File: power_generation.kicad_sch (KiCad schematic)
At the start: 36 parts, among them J301 61300211121, J302 61300211121, J303 36103505, J304 36103505, U301 AP64500SP-13, U302 AP64500SP-13

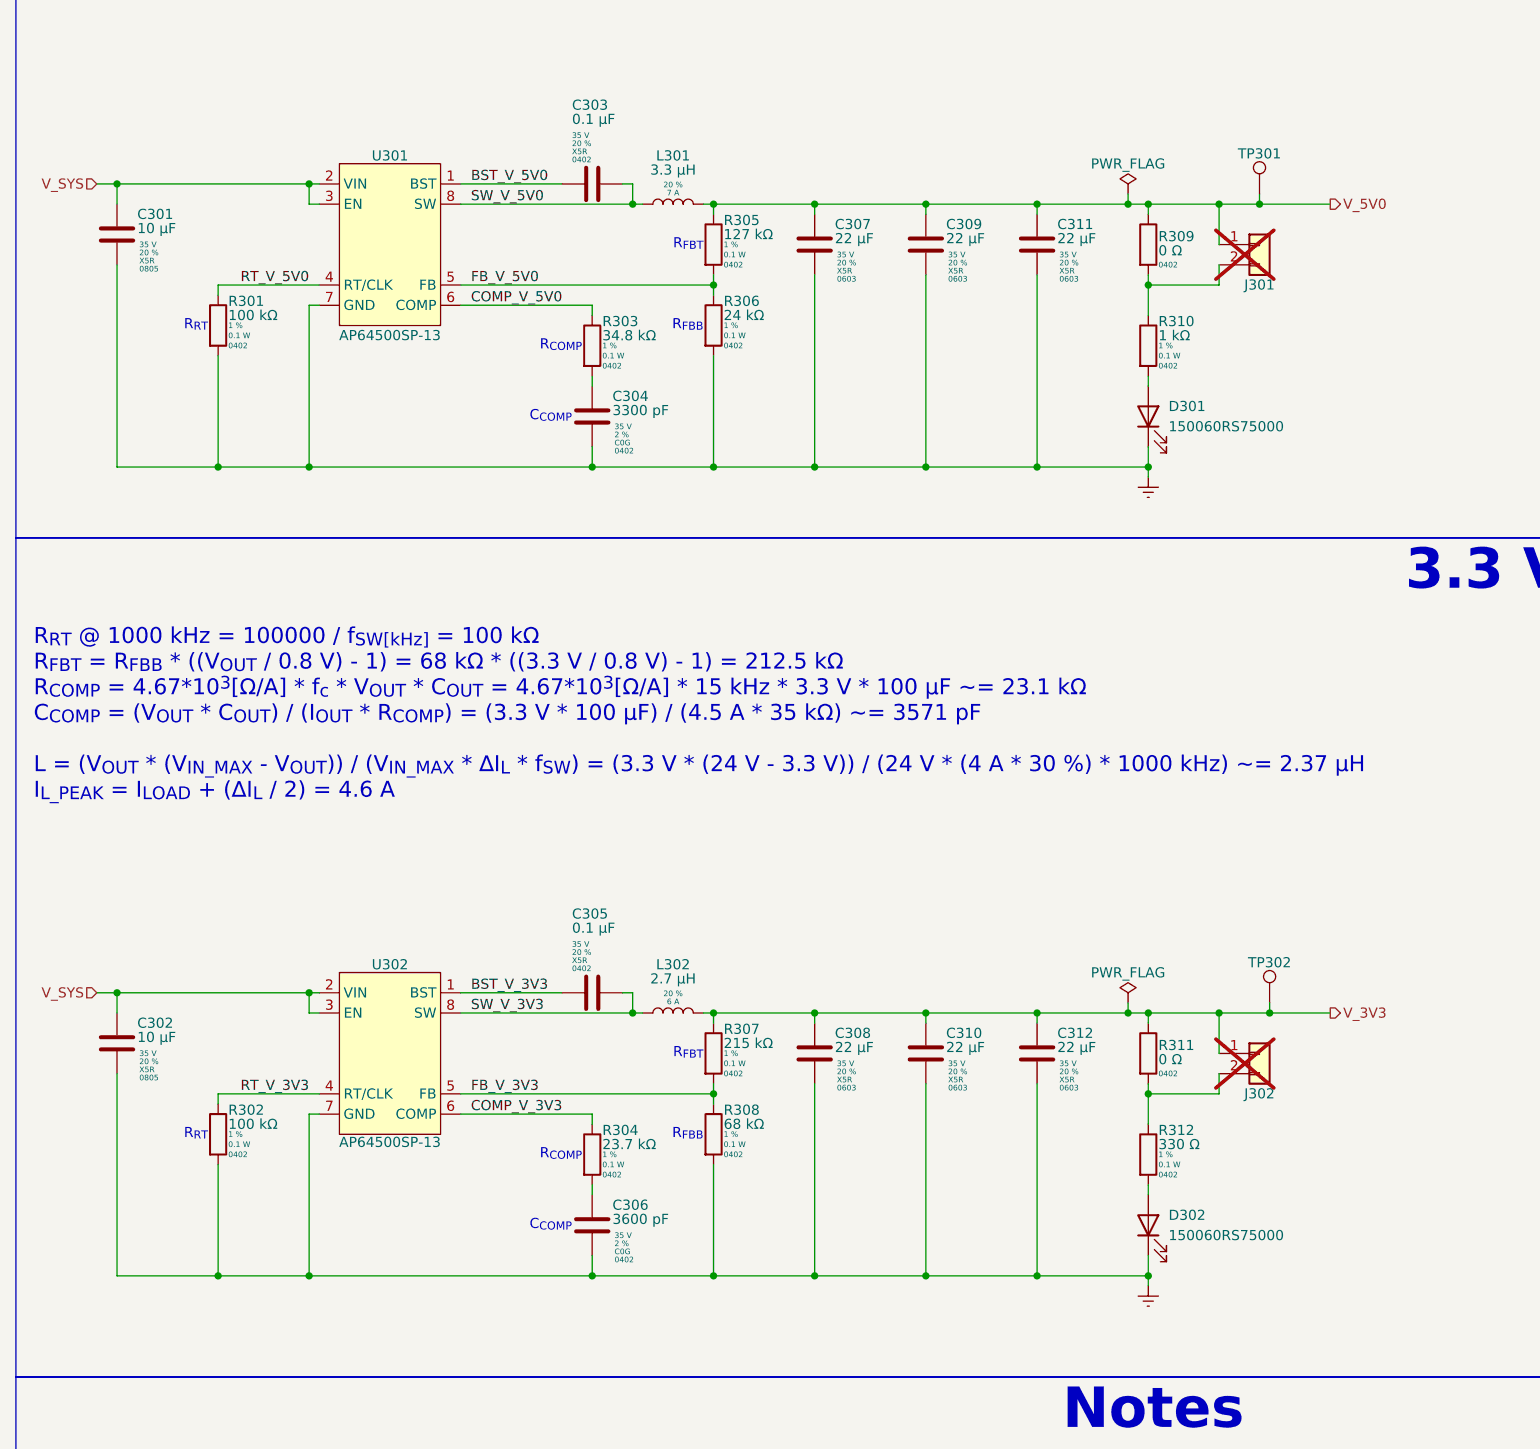
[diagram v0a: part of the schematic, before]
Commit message: Update capacitor BOM
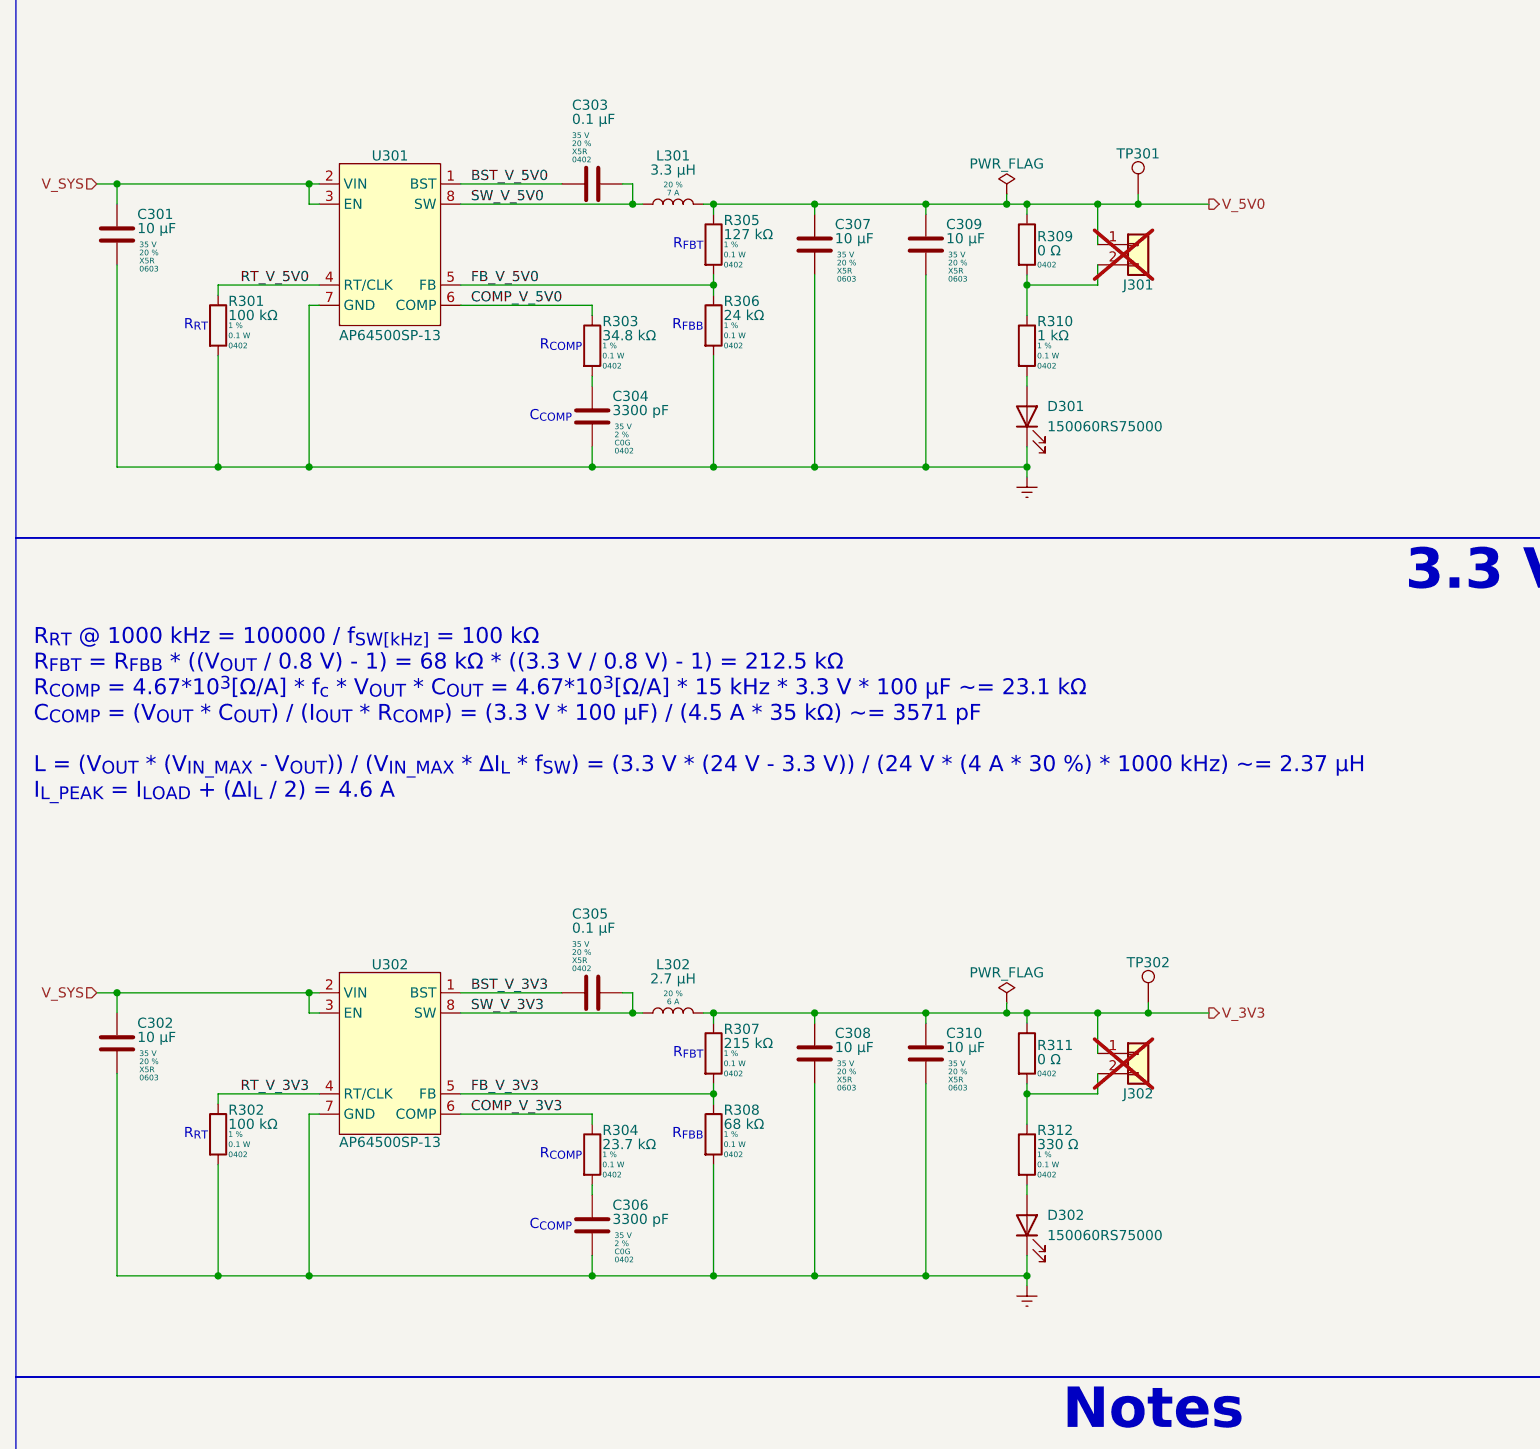
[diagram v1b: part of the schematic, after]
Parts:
- removed C311, C312: 22 µF, symbol Device:C
- C301, C302: footprint (none) -> Capacitor_SMD:C_0603_1608Metric; Digi-Key Part Number (none) -> 490-13248-1-ND; MPN (none) -> GRM188R6YA106MA73D; Manufacturer (none) -> Murata Electronics; Size 0805 -> 0603
- C303, C305: footprint (none) -> perfect_footprints:C_0402_1005Metric; Digi-Key Part Number (none) -> 490-10700-1-ND; MPN (none) -> GRM155R71H104KE14D; Manufacturer (none) -> Murata Electronics
- C304: footprint (none) -> perfect_footprints:C_0402_1005Metric; Digi-Key Part Number (none) -> 490-GRM1555C1H332GE01JCT-ND; MPN (none) -> GRM1555C1H332GE01J; Manufacturer (none) -> Murata Electronics
- C306: value 3600 pF -> 3300 pF; footprint (none) -> perfect_footprints:C_0402_1005Metric; Digi-Key Part Number (none) -> 490-GRM1555C1H332GE01JCT-ND; MPN (none) -> GRM1555C1H332GE01J; Manufacturer (none) -> Murata Electronics
- C307, C308, C309, C310: value 22 µF -> 10 µF; footprint (none) -> Capacitor_SMD:C_0603_1608Metric; Digi-Key Part Number (none) -> 490-13248-1-ND; MPN (none) -> GRM188R6YA106MA73D; Manufacturer (none) -> Murata Electronics
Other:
- moved on the sheet: D301, D302, J301, J302, R309, R310, R311, R312, TP301, TP302

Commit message: Update R & L BOM
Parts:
- L301: footprint (none) -> Inductor_SMD:L_Chilisin_BMRx00060630
- L302: footprint (none) -> Inductor_SMD:L_Bourns-SRN8040_8x8.15mm; Digi-Key Part Number 308-CDRH125L125NP-2R7NCCT-ND -> 118-SRN8040HA-2R7MCT-ND; MPN CDRH125L125NP-2R7NC -> SRN8040HA-2R7M; Manufacturer Sumida America Components Inc. -> Bourns Inc.
- R301, R302: Digi-Key Part Number (none) -> P100KLCT-ND; MPN (none) -> ERJ-2RKF1003X; Manufacturer (none) -> Panasonic Electronic Components
- R303: Digi-Key Part Number (none) -> P34.8KLCT-ND; MPN (none) -> ERJ-2RKF3482X; Manufacturer (none) -> Panasonic Electronic Components
- R304: Digi-Key Part Number (none) -> P23.7KLCT-ND; MPN (none) -> ERJ-2RKF2372X; Manufacturer (none) -> Panasonic Electronic Components
- R305: Digi-Key Part Number (none) -> P127KLCT-ND; MPN (none) -> ERJ-2RKF1273X; Manufacturer (none) -> Panasonic Electronic Components
- R306: Digi-Key Part Number (none) -> 732-560112110178CT-ND; MPN (none) -> 560112110178; Manufacturer (none) -> Würth Elektronik
- R307: Digi-Key Part Number (none) -> P215KLCT-ND; MPN (none) -> ERJ-2RKF2153X; Manufacturer (none) -> Panasonic Electronic Components
- R308: Digi-Key Part Number (none) -> 732-560112110035CT-ND; MPN (none) -> 560112110035; Manufacturer (none) -> Würth Elektronik
- R309, R311: footprint (none) -> perfect_footprints:R_0402_1005Metric; Digi-Key Part Number (none) -> P0.0JCT-ND; MPN (none) -> ERJ-2GE0R00X; Manufacturer (none) -> Panasonic Electronic Components
- R310: Digi-Key Part Number (none) -> P1.00KLCT-ND; MPN (none) -> ERJ-2RKF1001X; Manufacturer (none) -> Panasonic Electronic Components
- R312: Digi-Key Part Number (none) -> 732-560112110231CT-ND; MPN (none) -> 560112110231; Manufacturer (none) -> Würth Elektronik

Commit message: Fill BOM info
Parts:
- D301, D302: Digi-Key Part Number (none) -> 732-4978-1-ND
- J301, J302: Digi-Key Part Number (none) -> 732-5315-ND
- J303, J304: footprint (none) -> RF_Shielding:Wuerth_36103205_20x20mm
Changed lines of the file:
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@@
 			)
 		)
+		(property "Digi-Key Part Number" "732-5315-ND"
+			(at 153.67 109.22 0)
+			(effects
+				(font
+					(size 1.27 1.27)
+				)
+				(hide yes)
+			)
+		)
 		(pin "2"
 		)
@@
 			)
 		)
-		(property "Footprint" ""
+		(property "Footprint" "RF_Shielding:Wuerth_36103205_20x20mm"
 			(at 228.6 104.14 0)
 			(effects
@@
 			)
 		)
-		(property "Footprint" ""
+		(property "Footprint" "RF_Shielding:Wuerth_36103205_20x20mm"
 			(at 228.6 205.74 0)
 			(effects
@@
 			)
 		)
+		(property "Digi-Key Part Number" "732-5315-ND"
+			(at 153.67 210.82 0)
+			(effects
+				(font
+					(size 1.27 1.27)
+				)
+				(hide yes)
+			)
+		)
 		(pin "2"
 		)
@@
 			)
 		)
+		(property "Digi-Key Part Number" "732-4978-1-ND"
+			(at 139.7 130.81 90)
+			(effects
+				(font
+					(size 1.27 1.27)
+				)
+				(hide yes)
+			)
+		)
 		(pin "2"
 		)
@@
 			(effects
 				(font
+					(size 1.27 1.27)
+				)
+				(hide yes)
+			)
+		)
+		(property "Digi-Key Part Number" "732-4978-1-ND"
+			(at 139.7 232.41 90)
+			(effects
+				(font

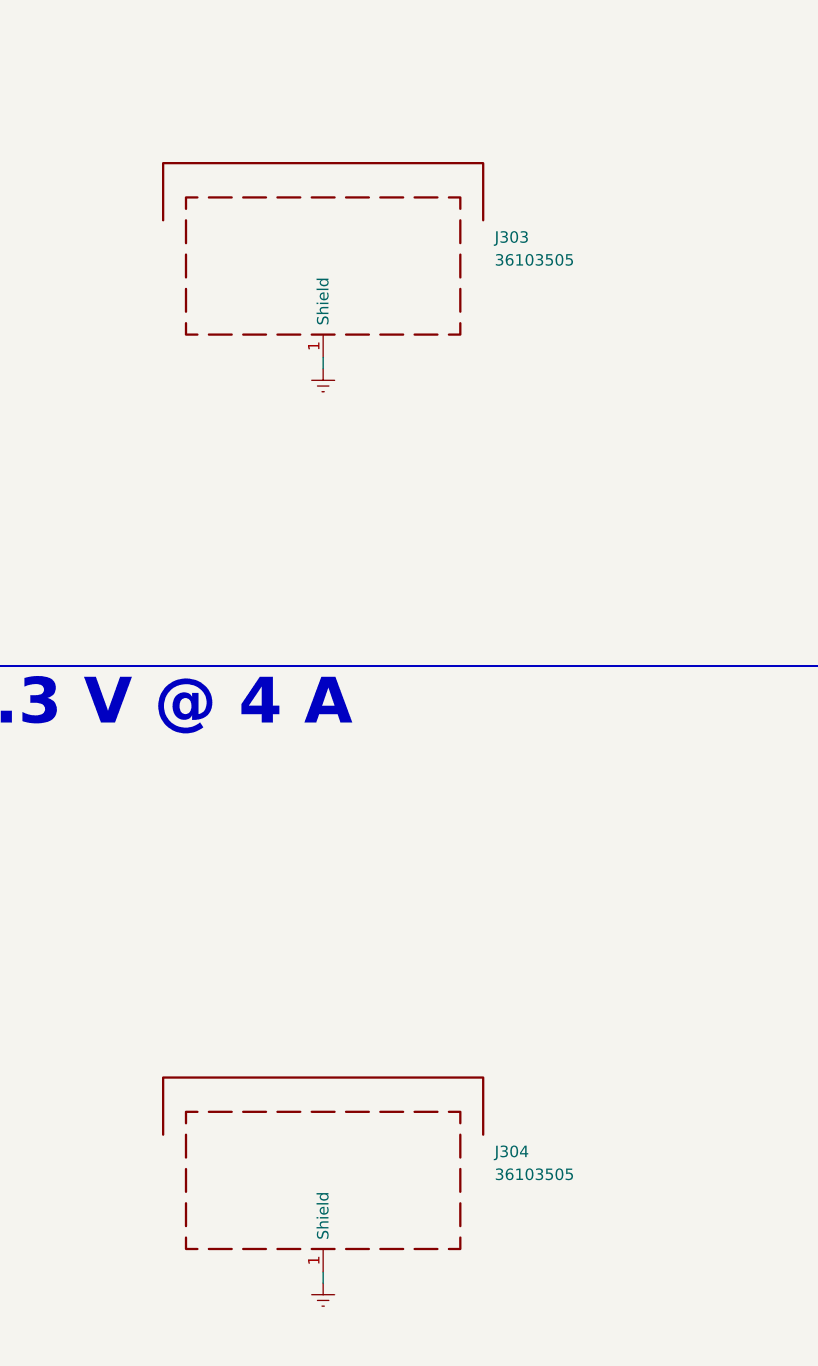
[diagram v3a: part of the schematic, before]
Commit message: Fill BOM information for the rest
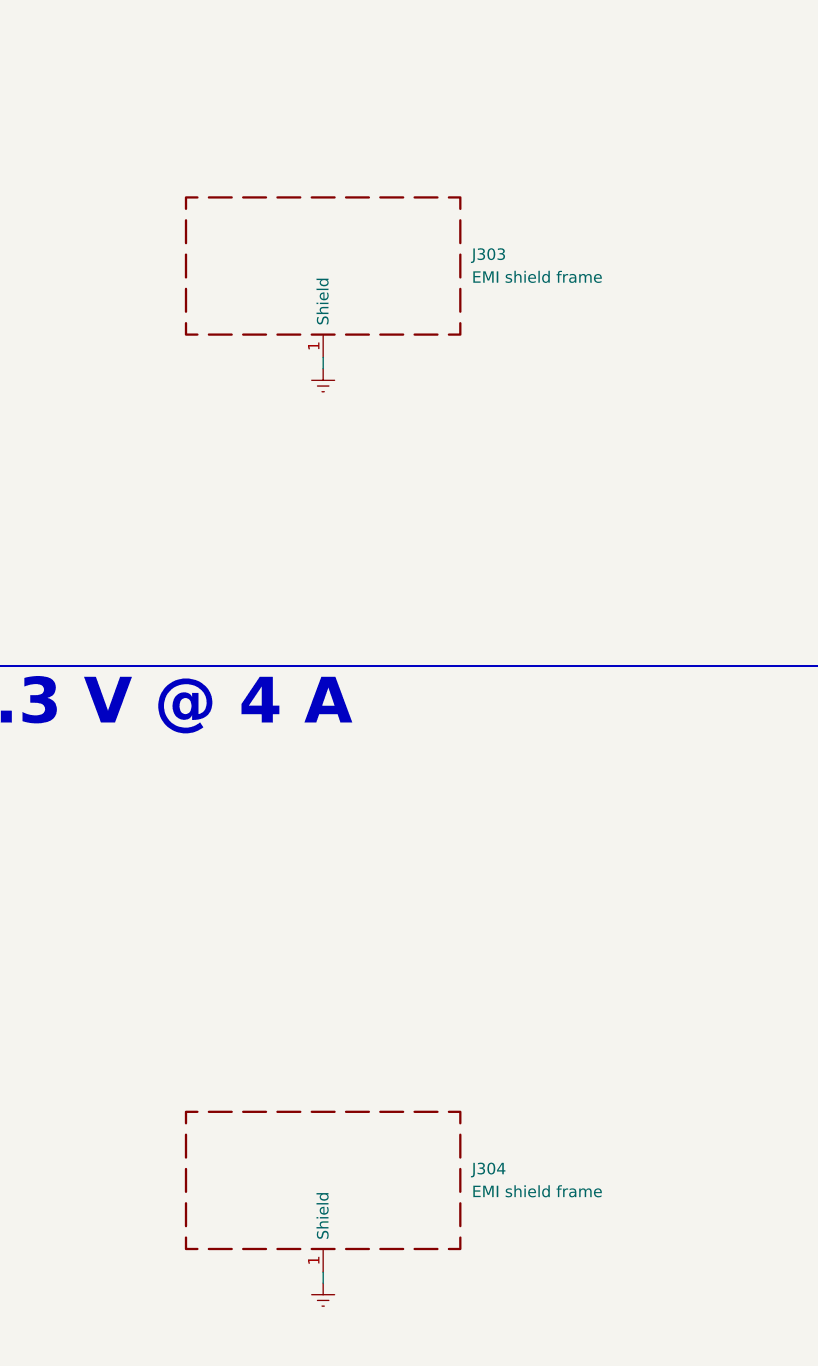
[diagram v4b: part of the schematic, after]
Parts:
- J303, J304: value 36103505 -> EMI shield frame; footprint RF_Shielding:Wuerth_36103205_20x20mm -> RF_Shielding:Laird_Technologies_BMI-S-202-F_16.50x16.50mm; symbol Device:RFShield_TwoPieces -> Device:RFShield_OnePiece; Digi-Key Part Number (none) -> 903-1051-1-ND; MPN (none) -> BMI-S-202-F; Manufacturer (none) -> Laird Technologies EMI
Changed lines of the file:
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@@
 	)
 	(symbol
-		(lib_id "Device:RFShield_TwoPieces")
+		(lib_id "Device:RFShield_OnePiece")
 		(at 228.6 101.6 0)
 		(unit 1)
@@
 		(fields_autoplaced yes)
 		(property "Reference" "J303"
-			(at 247.65 98.4249 0)
-			(effects
-				(font
-					(size 1.27 1.27)
-				)
-				(justify left)
-			)
-		)
-		(property "Value" "36103505"
-			(at 247.65 100.9649 0)
-			(effects
-				(font
-					(size 1.27 1.27)
-				)
-				(justify left)
-			)
-		)
-		(property "Footprint" "RF_Shielding:Wuerth_36103205_20x20mm"
+			(at 245.11 100.3299 0)
+			(effects
+				(font
+					(size 1.27 1.27)
+				)
+				(justify left)
+			)
+		)
+		(property "Value" "EMI shield frame"
+			(at 245.11 102.8699 0)
+			(effects
+				(font
+					(size 1.27 1.27)
+				)
+				(justify left)
+			)
+		)
+		(property "Footprint" "RF_Shielding:Laird_Technologies_BMI-S-202-F_16.50x16.50mm"
 			(at 228.6 104.14 0)
 			(effects
@@
 			)
 		)
-		(property "Datasheet" "https://www.we-online.com/components/products/datasheet/36103505.pdf"
+		(property "Datasheet" "~"
 			(at 228.6 104.14 0)
 			(effects
@@
 			)
 		)
-		(property "Description" "Two-piece EMI RF shielding cabinet"
+		(property "Description" "One-piece EMI RF shielding cabinet"
+			(at 228.6 101.6 0)
+			(effects
+				(font
+					(size 1.27 1.27)
+				)
+				(hide yes)
+			)
+		)
+		(property "Digi-Key Part Number" "903-1051-1-ND"
+			(at 228.6 101.6 0)
+			(effects
+				(font
+					(size 1.27 1.27)
+				)
+				(hide yes)
+			)
+		)
+		(property "MPN" "BMI-S-202-F"
+			(at 228.6 101.6 0)
+			(effects
+				(font
+					(size 1.27 1.27)
+				)
+				(hide yes)
+			)
+		)
+		(property "Manufacturer" "Laird Technologies EMI"
 			(at 228.6 101.6 0)
 			(effects
@@
 	)
 	(symbol
-		(lib_id "Device:RFShield_TwoPieces")
+		(lib_id "Device:RFShield_OnePiece")
 		(at 228.6 203.2 0)
 		(unit 1)
@@
 		(fields_autoplaced yes)
 		(property "Reference" "J304"
-			(at 247.65 200.0249 0)
-			(effects
-				(font
-					(size 1.27 1.27)
-				)
-				(justify left)
-			)
-		)
-		(property "Value" "36103505"
-			(at 247.65 202.5649 0)
-			(effects
-				(font
-					(size 1.27 1.27)
-				)
-				(justify left)
-			)
-		)
-		(property "Footprint" "RF_Shielding:Wuerth_36103205_20x20mm"
+			(at 245.11 201.9299 0)
+			(effects
+				(font
+					(size 1.27 1.27)
+				)
+				(justify left)
+			)
+		)
+		(property "Value" "EMI shield frame"
+			(at 245.11 204.4699 0)
+			(effects
+				(font
+					(size 1.27 1.27)
+				)
+				(justify left)
+			)
+		)
+		(property "Footprint" "RF_Shielding:Laird_Technologies_BMI-S-202-F_16.50x16.50mm"
 			(at 228.6 205.74 0)
 			(effects
@@
 			)
 		)
-		(property "Datasheet" "https://www.we-online.com/components/products/datasheet/36103505.pdf"
+		(property "Datasheet" "~"
 			(at 228.6 205.74 0)
 			(effects
@@
 			)
 		)
-		(property "Description" "Two-piece EMI RF shielding cabinet"
+		(property "Description" "One-piece EMI RF shielding cabinet"
 			(at 228.6 203.2 0)
 			(effects
+				(font
+					(size 1.27 1.27)
+				)
+				(hide yes)
+			)
+		)
+		(property "Digi-Key Part Number" "903-1051-1-ND"
+			(at 228.6 203.2 0)
+			(effects
+				(font
+					(size 1.27 1.27)
+				)
+				(hide yes)
+			)
+		)
+		(property "MPN" "BMI-S-202-F"
+			(at 228.6 203.2 0)
+			(effects
+				(font
+					(size 1.27 1.27)
+				)
+				(hide yes)
+			)
+		)
+		(property "Manufacturer" "Laird Technologies EMI"
+			(at 228.6 203.2 0)
+			(effects
